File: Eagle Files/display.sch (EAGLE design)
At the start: 16 parts, among them CN1 Charger, IC1 ATMEGA 328P-PU

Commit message: removed one button
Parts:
- removed JP6: PWM, adafruit:PINHD-1X1CB
- removed S4: (no value), switch-omron:10-XX
- S3: MPN (none) -> B3F-1000; OC_FARNELL (none) -> 176432; OC_NEWARK (none) -> 36M3542
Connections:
- removed net N$23: IC1.PB3(MOSI/OC2), JP6.1
- removed net N$9: IC1.PB2(SS/OC1B), S3.P1
- net N$13: no longer S4.S
- net N$17: now also S3.P1; no longer S4.P1
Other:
- moved on the sheet: S3
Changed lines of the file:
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@@
 <part name="S1" library="switch-omron" deviceset="10-XX" device=""/>
 <part name="S2" library="switch-omron" deviceset="10-XX" device=""/>
-<part name="S3" library="switch-omron" deviceset="10-XX" device=""/>
 <part name="R2" library="rcl" deviceset="R-EU_" device="0204/7" value="100"/>
-<part name="S4" library="switch-omron" deviceset="10-XX" device="">
+<part name="S3" library="switch-omron" deviceset="10-XX" device="">
 <attribute name="MF" value=""/>
 <attribute name="MPN" value="B3F-1000"/>
@@
 <part name="JP5" library="pinhead" deviceset="PINHD-1X2" device="" value="Power"/>
 <part name="JP4" library="adafruit" deviceset="PINHD-1X6" device="CLEAN" value="Ananlog IO"/>
-<part name="JP6" library="adafruit" deviceset="PINHD-1X1" device="CB" value="PWM"/>
 </parts>
 <sheets>
@@
 <instance part="S1" gate="1" x="38.1" y="22.86"/>
 <instance part="S2" gate="1" x="20.32" y="22.86"/>
-<instance part="S3" gate="1" x="10.16" y="5.08"/>
 <instance part="R2" gate="G$1" x="22.86" y="33.02" rot="R180"/>
-<instance part="S4" gate="1" x="30.48" y="5.08"/>
+<instance part="S3" gate="1" x="30.48" y="5.08"/>
 <instance part="C1" gate="G$1" x="43.18" y="78.74"/>
 <instance part="JP2" gate="A" x="129.54" y="50.8"/>
@@
 <instance part="JP5" gate="G$1" x="-7.62" y="40.64"/>
 <instance part="JP4" gate="A" x="114.3" y="66.04"/>
-<instance part="JP6" gate="G$1" x="132.08" y="25.4"/>
 </instances>
 <busses>
@@
 <pinref part="IC1" gate="G$1" pin="PD7(AIN1)"/>
 <wire x1="66.04" y1="33.02" x2="91.44" y2="33.02" width="0.1524" layer="91"/>
-</segment>
-</net>
-<net name="N$9" class="0">
-<segment>
-<pinref part="S3" gate="1" pin="P1"/>
-<wire x1="12.7" y1="0" x2="17.78" y2="0" width="0.1524" layer="91"/>
-<wire x1="17.78" y1="0" x2="17.78" y2="12.7" width="0.1524" layer="91"/>
-<wire x1="17.78" y1="12.7" x2="91.44" y2="12.7" width="0.1524" layer="91"/>
-<pinref part="IC1" gate="G$1" pin="PB2(SS/OC1B)"/>
-<wire x1="91.44" y1="12.7" x2="91.44" y2="22.86" width="0.1524" layer="91"/>
 </segment>
 </net>
@@
 <net name="N$13" class="0">
 <segment>
-<pinref part="S3" gate="1" pin="S"/>
-<wire x1="10.16" y1="10.16" x2="10.16" y2="33.02" width="0.1524" layer="91"/>
 <pinref part="R2" gate="G$1" pin="2"/>
-<wire x1="10.16" y1="33.02" x2="17.78" y2="33.02" width="0.1524" layer="91"/>
-<junction x="17.78" y="33.02"/>
 <wire x1="17.78" y1="33.02" x2="17.78" y2="30.48" width="0.1524" layer="91"/>
 <wire x1="17.78" y1="30.48" x2="20.32" y2="30.48" width="0.1524" layer="91"/>
@@
 <pinref part="S2" gate="1" pin="S"/>
 <wire x1="20.32" y1="30.48" x2="20.32" y2="27.94" width="0.1524" layer="91"/>
-<pinref part="S4" gate="1" pin="S"/>
+<pinref part="S3" gate="1" pin="S"/>
 <wire x1="30.48" y1="10.16" x2="30.48" y2="30.48" width="0.1524" layer="91"/>
 <junction x="20.32" y="30.48"/>
@@
 <segment>
 <wire x1="93.98" y1="27.94" x2="93.98" y2="0" width="0.1524" layer="91"/>
-<pinref part="S4" gate="1" pin="P1"/>
+<pinref part="S3" gate="1" pin="P1"/>
 <wire x1="93.98" y1="0" x2="33.02" y2="0" width="0.1524" layer="91"/>
 <pinref part="IC1" gate="G$1" pin="PB0(ICP)"/>
@@
 </segment>
 </net>
-<net name="N$23" class="0">
-<segment>
-<pinref part="IC1" gate="G$1" pin="PB3(MOSI/OC2)"/>
-<wire x1="91.44" y1="20.32" x2="124.46" y2="20.32" width="0.1524" layer="91"/>
-<wire x1="124.46" y1="20.32" x2="124.46" y2="25.4" width="0.1524" layer="91"/>
-<pinref part="JP6" gate="G$1" pin="1"/>
-<wire x1="124.46" y1="25.4" x2="129.54" y2="25.4" width="0.1524" layer="91"/>
-</segment>
-</net>

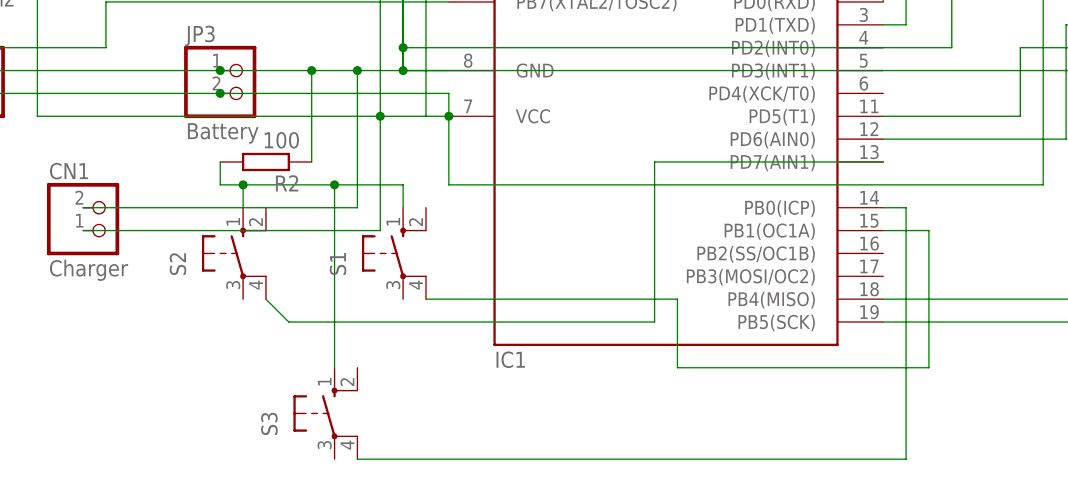
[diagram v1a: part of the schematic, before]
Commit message: changed labes and positioning
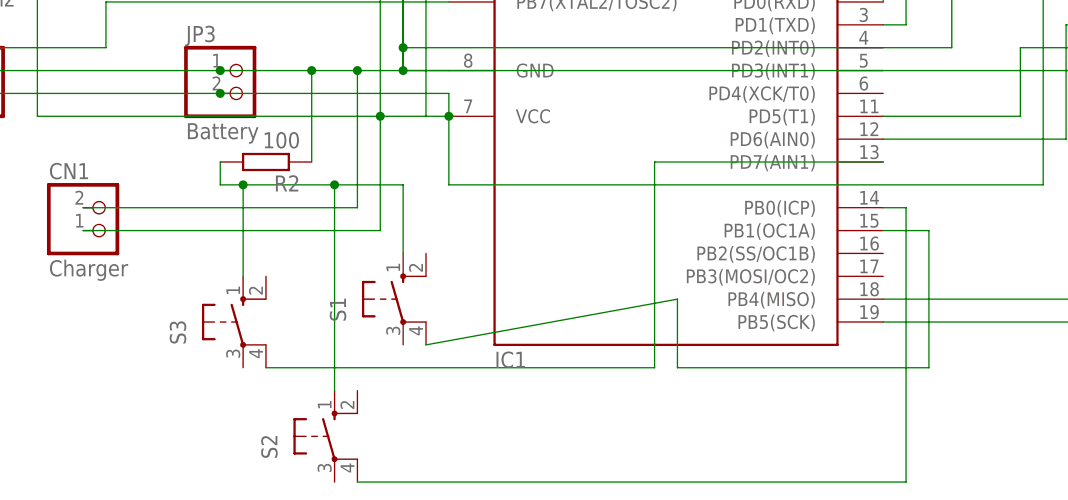
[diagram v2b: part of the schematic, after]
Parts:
- S2: MPN (none) -> B3F-1000; OC_FARNELL (none) -> 176432; OC_NEWARK (none) -> 36M3542
- S3: MPN B3F-1000 -> (none); OC_FARNELL 176432 -> (none); OC_NEWARK 36M3542 -> (none)
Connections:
- net N$11: now also S3.P1; no longer S2.P1
- net N$17: now also S2.P1; no longer S3.P1
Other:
- moved on the sheet: S1, S2, S3
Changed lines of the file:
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@@
 <part name="JP3" library="pinhead" deviceset="PINHD-1X2" device="" value="Battery"/>
 <part name="S1" library="switch-omron" deviceset="10-XX" device=""/>
-<part name="S2" library="switch-omron" deviceset="10-XX" device=""/>
+<part name="S3" library="switch-omron" deviceset="10-XX" device=""/>
 <part name="R2" library="rcl" deviceset="R-EU_" device="0204/7" value="100"/>
-<part name="S3" library="switch-omron" deviceset="10-XX" device="">
+<part name="S2" library="switch-omron" deviceset="10-XX" device="">
 <attribute name="MF" value=""/>
 <attribute name="MPN" value="B3F-1000"/>
@@
 <instance part="JP1" gate="A" x="22.86" y="66.04"/>
 <instance part="JP3" gate="G$1" x="20.32" y="40.64"/>
-<instance part="S1" gate="1" x="38.1" y="22.86"/>
-<instance part="S2" gate="1" x="20.32" y="22.86"/>
+<instance part="S1" gate="1" x="38.1" y="17.78"/>
+<instance part="S3" gate="1" x="20.32" y="15.24"/>
 <instance part="R2" gate="G$1" x="22.86" y="33.02" rot="R180"/>
-<instance part="S3" gate="1" x="30.48" y="5.08"/>
+<instance part="S2" gate="1" x="30.48" y="2.54"/>
 <instance part="C1" gate="G$1" x="43.18" y="78.74"/>
 <instance part="JP2" gate="A" x="129.54" y="50.8"/>
@@
 <segment>
 <pinref part="S1" gate="1" pin="P1"/>
-<wire x1="40.64" y1="17.78" x2="68.58" y2="17.78" width="0.1524" layer="91"/>
+<wire x1="40.64" y1="12.7" x2="68.58" y2="17.78" width="0.1524" layer="91"/>
 <wire x1="68.58" y1="17.78" x2="68.58" y2="10.16" width="0.1524" layer="91"/>
 <wire x1="68.58" y1="10.16" x2="96.52" y2="10.16" width="0.1524" layer="91"/>
@@
 <net name="N$11" class="0">
 <segment>
-<pinref part="S2" gate="1" pin="P1"/>
-<wire x1="22.86" y1="17.78" x2="25.4" y2="15.24" width="0.1524" layer="91"/>
-<wire x1="25.4" y1="15.24" x2="66.04" y2="15.24" width="0.1524" layer="91"/>
-<wire x1="66.04" y1="15.24" x2="66.04" y2="33.02" width="0.1524" layer="91"/>
+<pinref part="S3" gate="1" pin="P1"/>
+<wire x1="22.86" y1="10.16" x2="66.04" y2="10.16" width="0.1524" layer="91"/>
+<wire x1="66.04" y1="10.16" x2="66.04" y2="33.02" width="0.1524" layer="91"/>
 <pinref part="IC1" gate="G$1" pin="PD7(AIN1)"/>
 <wire x1="66.04" y1="33.02" x2="91.44" y2="33.02" width="0.1524" layer="91"/>
@@
 <wire x1="20.32" y1="30.48" x2="30.48" y2="30.48" width="0.1524" layer="91"/>
 <wire x1="30.48" y1="30.48" x2="38.1" y2="30.48" width="0.1524" layer="91"/>
-<wire x1="38.1" y1="30.48" x2="38.1" y2="27.94" width="0.1524" layer="91"/>
+<wire x1="38.1" y1="30.48" x2="38.1" y2="22.86" width="0.1524" layer="91"/>
+<pinref part="S3" gate="1" pin="S"/>
+<wire x1="20.32" y1="30.48" x2="20.32" y2="20.32" width="0.1524" layer="91"/>
 <pinref part="S2" gate="1" pin="S"/>
-<wire x1="20.32" y1="30.48" x2="20.32" y2="27.94" width="0.1524" layer="91"/>
-<pinref part="S3" gate="1" pin="S"/>
-<wire x1="30.48" y1="10.16" x2="30.48" y2="30.48" width="0.1524" layer="91"/>
+<wire x1="30.48" y1="7.62" x2="30.48" y2="30.48" width="0.1524" layer="91"/>
 <junction x="20.32" y="30.48"/>
 <junction x="30.48" y="30.48"/>
@@
 <net name="N$17" class="0">
 <segment>
-<wire x1="93.98" y1="27.94" x2="93.98" y2="0" width="0.1524" layer="91"/>
-<pinref part="S3" gate="1" pin="P1"/>
-<wire x1="93.98" y1="0" x2="33.02" y2="0" width="0.1524" layer="91"/>
+<wire x1="93.98" y1="27.94" x2="93.98" y2="-2.54" width="0.1524" layer="91"/>
+<pinref part="S2" gate="1" pin="P1"/>
+<wire x1="93.98" y1="-2.54" x2="33.02" y2="-2.54" width="0.1524" layer="91"/>
 <pinref part="IC1" gate="G$1" pin="PB0(ICP)"/>
 <wire x1="93.98" y1="27.94" x2="91.44" y2="27.94" width="0.1524" layer="91"/>

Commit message: fixed a typo
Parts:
- JP4: value Ananlog IO -> Analog IO
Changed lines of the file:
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@@
 <part name="CN1" library="adafruit" deviceset="JST_2PIN" device="-THM-RA" value="Charger"/>
 <part name="JP5" library="pinhead" deviceset="PINHD-1X2" device="" value="Power"/>
-<part name="JP4" library="adafruit" deviceset="PINHD-1X6" device="CLEAN" value="Ananlog IO"/>
+<part name="JP4" library="adafruit" deviceset="PINHD-1X6" device="CLEAN" value="Analog IO"/>
 </parts>
 <sheets>
